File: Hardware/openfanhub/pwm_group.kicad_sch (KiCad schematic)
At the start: 5 parts, among them Q3 Q_NMOS_GSD, Q4 AO449

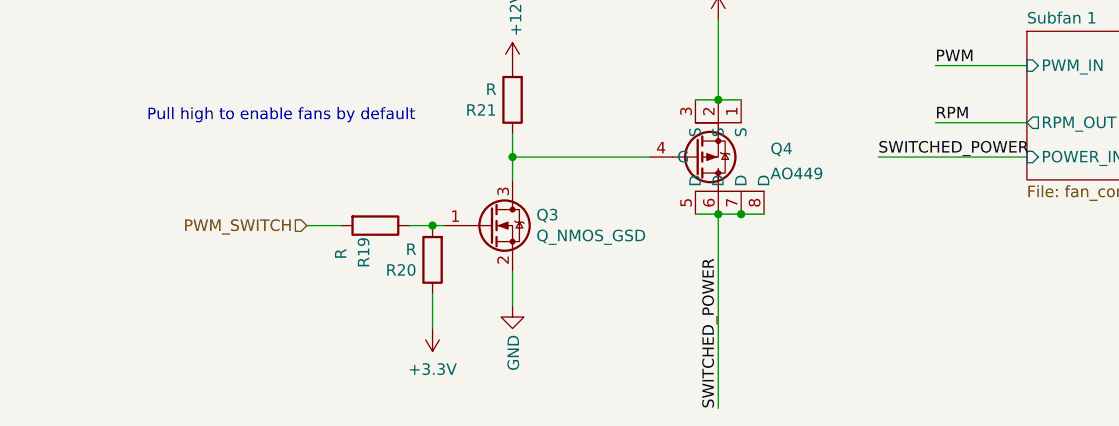
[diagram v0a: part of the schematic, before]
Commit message: Update PCB. Move Power and USB to the same side
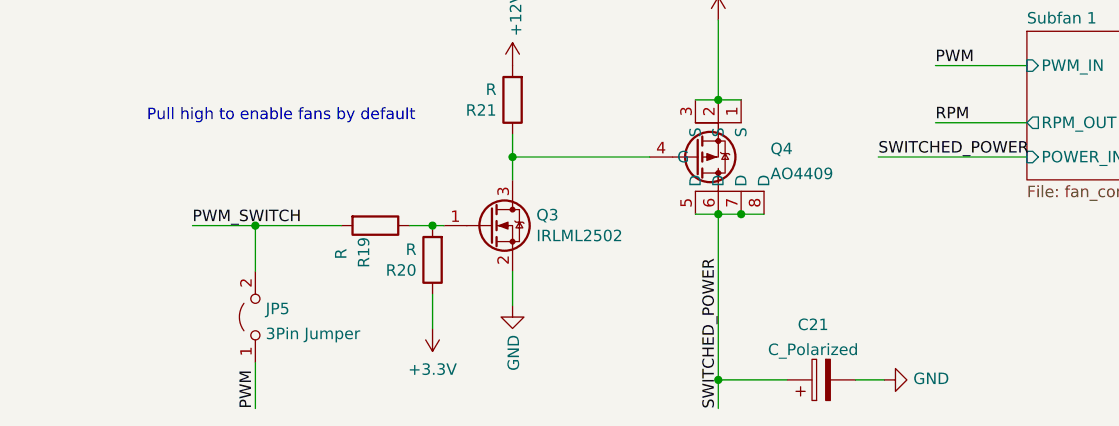
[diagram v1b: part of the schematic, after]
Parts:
- added C21: C_Polarized, Capacitor_THT:CP_Radial_D6.3mm_P2.50mm, symbol Device:C_Polarized
- added JP5: 3Pin Jumper, Connector_PinHeader_2.54mm:PinHeader_1x02_P2.54mm_Vertical, symbol Jumper:Jumper_2_Open
- Q3: value Q_NMOS_GSD -> IRLML2502
- Q4: value AO449 -> AO4409
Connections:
- net GND: now also C21.2
- net PWM: now also JP5.1 (A)
- net PWM_SWITCH: now also JP5.2 (B)
- net SWITCHED_POWER: now also C21.1
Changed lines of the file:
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@@
   (junction (at 71.12 58.42) (diameter 0) (color 0 0 0 0)
+  )
+  (junction (at 93.98 83.185) (diameter 0) (color 0 0 0 0)
+  )
+  (junction (at 42.545 66.04) (diameter 0) (color 0 0 0 0)
   )
   (junction (at 93.98 64.77) (diameter 0) (color 0 0 0 0)
@@
   (no_connect (at 170.18 55.88))
   (no_connect (at 213.36 55.88))
+  (wire (pts (xy 93.98 83.185) (xy 93.98 86.36))
+    (stroke (width 0) (type default) (color 0 0 0 0))
+  )
   (wire (pts (xy 152.4 59.69) (xy 170.18 59.69))
     (stroke (width 0) (type default) (color 0 0 0 0))
@@
     (stroke (width 0) (type default) (color 0 0 0 0))
   )
+  (wire (pts (xy 42.545 66.04) (xy 52.07 66.04))
+    (stroke (width 0) (type default) (color 0 0 0 0))
+  )
   (wire (pts (xy 93.98 52.07) (xy 96.52 52.07))
     (stroke (width 0) (type default) (color 0 0 0 0))
@@
     (stroke (width 0) (type default) (color 0 0 0 0))
   )
+  (wire (pts (xy 42.545 81.28) (xy 42.545 86.36))
+    (stroke (width 0) (type default) (color 0 0 0 0))
+  )
   (wire (pts (xy 111.76 58.42) (xy 128.27 58.42))
     (stroke (width 0) (type default) (color 0 0 0 0))
   )
-  (wire (pts (xy 48.26 66.04) (xy 52.07 66.04))
-    (stroke (width 0) (type default) (color 0 0 0 0))
-  )
-  (wire (pts (xy 93.98 64.77) (xy 93.98 86.36))
+  (wire (pts (xy 35.56 66.04) (xy 42.545 66.04))
+    (stroke (width 0) (type default) (color 0 0 0 0))
+  )
+  (wire (pts (xy 109.22 83.185) (xy 112.395 83.185))
+    (stroke (width 0) (type default) (color 0 0 0 0))
+  )
+  (wire (pts (xy 93.98 64.77) (xy 93.98 83.185))
     (stroke (width 0) (type default) (color 0 0 0 0))
   )
@@
     (stroke (width 0) (type default) (color 0 0 0 0))
   )
+  (wire (pts (xy 42.545 66.04) (xy 42.545 71.12))
+    (stroke (width 0) (type default) (color 0 0 0 0))
+  )
   (wire (pts (xy 162.56 49.53) (xy 170.18 49.53))
     (stroke (width 0) (type default) (color 0 0 0 0))
@@
     (stroke (width 0) (type default) (color 0 0 0 0))
   )
+  (wire (pts (xy 93.98 83.185) (xy 101.6 83.185))
+    (stroke (width 0) (type default) (color 0 0 0 0))
+  )
   (wire (pts (xy 93.98 43.18) (xy 93.98 52.07))
     (stroke (width 0) (type default) (color 0 0 0 0))
@@
   )
   (label "RPM" (at 118.11 54.61 0)
-    (effects (font (size 1.27 1.27)) (justify left bottom))
-  )
-  (label "SWITCHED_POWER" (at 93.98 86.36 90)
-    (effects (font (size 1.27 1.27)) (justify left bottom))
-  )
-  (label "SWITCHED_POWER" (at 194.31 59.69 0)
     (effects (font (size 1.27 1.27)) (justify left bottom))
   )
@@
     (effects (font (size 1.27 1.27)) (justify right bottom))
   )
+  (label "SWITCHED_POWER" (at 93.98 86.36 90)
+    (effects (font (size 1.27 1.27)) (justify left bottom))
+  )
+  (label "SWITCHED_POWER" (at 194.31 59.69 0)
+    (effects (font (size 1.27 1.27)) (justify left bottom))
+  )
+  (label "PWM_SWITCH" (at 35.56 66.04 0)
+    (effects (font (size 1.27 1.27)) (justify left bottom))
+  )
   (label "RPM" (at 41.91 24.13 180)
     (effects (font (size 1.27 1.27)) (justify right bottom))
@@
     (effects (font (size 1.27 1.27)) (justify right bottom))
   )
+  (label "PWM" (at 42.545 86.36 90)
+    (effects (font (size 1.27 1.27)) (justify left bottom))
+  )
   (label "PWM" (at 118.11 48.26 0)
     (effects (font (size 1.27 1.27)) (justify left bottom))
@@
     (effects (font (size 1.27 1.27)) (justify right))
   )
-  (hierarchical_label "PWM_SWITCH" (shape input) (at 48.26 66.04 180)
-    (effects (font (size 1.27 1.27)) (justify right))
-  )
   (symbol (lib_id "power:+12V") (at 93.98 43.18 0)
     (in_bom yes) (on_board yes)
-    (property "Reference" "#PWR086" (id 0) (at 93.98 46.99 0)
+    (property "Reference" "#PWR058" (id 0) (at 93.98 46.99 0)
       (effects (font (size 1.27 1.27)) hide)
     )
@@
   (symbol (lib_id "power:+12V") (at 71.12 48.26 0)
     (in_bom yes) (on_board yes)
-    (property "Reference" "#PWR084" (id 0) (at 71.12 52.07 0)
+    (property "Reference" "#PWR056" (id 0) (at 71.12 52.07 0)
       (effects (font (size 1.27 1.27)) hide)
     )
@@
       (effects (font (size 1.27 1.27)) (justify left))
     )
-    (property "Value" "Q_NMOS_GSD" (id 1) (at 73.7616 67.183 0)
+    (property "Value" "IRLML2502" (id 1) (at 73.7616 67.183 0)
       (effects (font (size 1.27 1.27)) (justify left))
     )
@@
   (symbol (lib_id "power:GND") (at 71.12 74.93 0)
     (in_bom yes) (on_board yes)
-    (property "Reference" "#PWR085" (id 0) (at 71.12 81.28 0)
+    (property "Reference" "#PWR057" (id 0) (at 71.12 81.28 0)
       (effects (font (size 1.27 1.27)) hide)
     )
@@
     (pin "1")
     (pin "2")
+  )
+  (symbol (lib_id "power:GND") (at 112.395 83.185 90)
+    (in_bom yes) (on_board yes)
+    (property "Reference" "#PWR059" (id 0) (at 118.745 83.185 0)
+      (effects (font (size 1.27 1.27)) hide)
+    )
+    (property "Value" "GND" (id 1) (at 115.6462 83.058 90)
+      (effects (font (size 1.27 1.27)) (justify right))
+    )
+    (property "Footprint" "" (id 2) (at 112.395 83.185 0)
+      (effects (font (size 1.27 1.27)) hide)
+    )
+    (property "Datasheet" "" (id 3) (at 112.395 83.185 0)
+      (effects (font (size 1.27 1.27)) hide)
+    )
+    (pin "1")
   )
   (symbol (lib_id "my_components:AO449") (at 82.55 63.5 0) (mirror x)
@@
       (effects (font (size 1.27 1.27)) (justify left))
     )
-    (property "Value" "AO449" (id 1) (at 99.7712 60.2866 0)
+    (property "Value" "AO4409" (id 1) (at 99.7712 60.2866 0)
       (effects (font (size 1.27 1.27)) (justify left))
     )
@@
   (symbol (lib_id "power:+3.3V") (at 62.23 77.47 180)
     (in_bom yes) (on_board yes) (fields_autoplaced)
-    (property "Reference" "#PWR083" (id 0) (at 62.23 73.66 0)
+    (property "Reference" "#PWR055" (id 0) (at 62.23 73.66 0)
       (effects (font (size 1.27 1.27)) hide)
     )
@@
     (pin "1")
   )
+  (symbol (lib_id "Device:C_Polarized") (at 105.41 83.185 90)
+    (in_bom yes) (on_board yes) (fields_autoplaced)
+    (property "Reference" "C21" (id 0) (at 104.521 77.0595 90))
+    (property "Value" "C_Polarized" (id 1) (at 104.521 79.8346 90))
+    (property "Footprint" "Capacitor_THT:CP_Radial_D6.3mm_P2.50mm" (id 2) (at 109.22 82.2198 0)
+      (effects (font (size 1.27 1.27)) hide)
+    )
+    (property "Datasheet" "~" (id 3) (at 105.41 83.185 0)
+      (effects (font (size 1.27 1.27)) hide)
+    )
+    (pin "1")
+    (pin "2")
+  )
+  (symbol (lib_id "Jumper:Jumper_2_Open") (at 42.545 76.2 90)
+    (in_bom yes) (on_board yes) (fields_autoplaced)
+    (property "Reference" "JP5" (id 0) (at 43.688 75.2915 90)
+      (effects (font (size 1.27 1.27)) (justify right))
+    )
+    (property "Value" "3Pin Jumper" (id 1) (at 43.688 78.0666 90)
+      (effects (font (size 1.27 1.27)) (justify right))
+    )
+    (property "Footprint" "Connector_PinHeader_2.54mm:PinHeader_1x02_P2.54mm_Vertical" (id 2) (at 42.545 76.2 0)
+      (effects (font (size 1.27 1.27)) hide)
+    )
+    (property "Datasheet" "~" (id 3) (at 42.545 76.2 0)
+      (effects (font (size 1.27 1.27)) hide)
+    )
+    (pin "1")
+    (pin "2")
+  )
   (sheet (at 128.27 44.45) (size 21.59 16.51) (fields_autoplaced)

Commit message: Update (not sure what)
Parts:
- renumbered C21 to C25, JP5 to JP9, Q3 to Q11, Q4 to Q12, R19 to R31, R20 to R32, R21 to R33
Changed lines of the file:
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@@
   (symbol (lib_id "power:+12V") (at 93.98 43.18 0)
     (in_bom yes) (on_board yes)
-    (property "Reference" "#PWR058" (id 0) (at 93.98 46.99 0)
+    (property "Reference" "#PWR090" (id 0) (at 93.98 46.99 0)
       (effects (font (size 1.27 1.27)) hide)
     )
@@
   (symbol (lib_id "Device:R") (at 55.88 66.04 270)
     (in_bom yes) (on_board yes)
-    (property "Reference" "R19" (id 0) (at 54.61 67.31 0)
+    (property "Reference" "R31" (id 0) (at 54.61 67.31 0)
       (effects (font (size 1.27 1.27)) (justify left))
     )
@@
   (symbol (lib_id "power:+12V") (at 71.12 48.26 0)
     (in_bom yes) (on_board yes)
-    (property "Reference" "#PWR056" (id 0) (at 71.12 52.07 0)
+    (property "Reference" "#PWR088" (id 0) (at 71.12 52.07 0)
       (effects (font (size 1.27 1.27)) hide)
     )
@@
   (symbol (lib_id "Device:Q_NMOS_GSD") (at 68.58 66.04 0)
     (in_bom yes) (on_board yes)
-    (property "Reference" "Q3" (id 0) (at 73.7616 64.8716 0)
+    (property "Reference" "Q11" (id 0) (at 73.7616 64.8716 0)
       (effects (font (size 1.27 1.27)) (justify left))
     )
@@
   (symbol (lib_id "Device:R") (at 71.12 52.07 180)
     (in_bom yes) (on_board yes)
-    (property "Reference" "R21" (id 0) (at 69.342 53.2384 0)
+    (property "Reference" "R33" (id 0) (at 69.342 53.2384 0)
       (effects (font (size 1.27 1.27)) (justify left))
     )
@@
   (symbol (lib_id "power:GND") (at 71.12 74.93 0)
     (in_bom yes) (on_board yes)
-    (property "Reference" "#PWR057" (id 0) (at 71.12 81.28 0)
+    (property "Reference" "#PWR089" (id 0) (at 71.12 81.28 0)
       (effects (font (size 1.27 1.27)) hide)
     )
@@
   (symbol (lib_id "Device:R") (at 62.23 69.85 180)
     (in_bom yes) (on_board yes)
-    (property "Reference" "R20" (id 0) (at 60.452 71.0184 0)
+    (property "Reference" "R32" (id 0) (at 60.452 71.0184 0)
       (effects (font (size 1.27 1.27)) (justify left))
     )
@@
   (symbol (lib_id "power:GND") (at 112.395 83.185 90)
     (in_bom yes) (on_board yes)
-    (property "Reference" "#PWR059" (id 0) (at 118.745 83.185 0)
+    (property "Reference" "#PWR091" (id 0) (at 118.745 83.185 0)
       (effects (font (size 1.27 1.27)) hide)
     )
@@
   (symbol (lib_id "my_components:AO449") (at 82.55 63.5 0) (mirror x)
     (in_bom yes) (on_board yes) (fields_autoplaced)
-    (property "Reference" "Q4" (id 0) (at 99.7712 57.5115 0)
+    (property "Reference" "Q12" (id 0) (at 99.7712 57.5115 0)
       (effects (font (size 1.27 1.27)) (justify left))
     )
@@
   (symbol (lib_id "power:+3.3V") (at 62.23 77.47 180)
     (in_bom yes) (on_board yes) (fields_autoplaced)
-    (property "Reference" "#PWR055" (id 0) (at 62.23 73.66 0)
+    (property "Reference" "#PWR087" (id 0) (at 62.23 73.66 0)
       (effects (font (size 1.27 1.27)) hide)
     )
@@
   (symbol (lib_id "Device:C_Polarized") (at 105.41 83.185 90)
     (in_bom yes) (on_board yes) (fields_autoplaced)
-    (property "Reference" "C21" (id 0) (at 104.521 77.0595 90))
+    (property "Reference" "C25" (id 0) (at 104.521 77.0595 90))
     (property "Value" "C_Polarized" (id 1) (at 104.521 79.8346 90))
     (property "Footprint" "Capacitor_THT:CP_Radial_D6.3mm_P2.50mm" (id 2) (at 109.22 82.2198 0)
@@
   (symbol (lib_id "Jumper:Jumper_2_Open") (at 42.545 76.2 90)
     (in_bom yes) (on_board yes) (fields_autoplaced)
-    (property "Reference" "JP5" (id 0) (at 43.688 75.2915 90)
+    (property "Reference" "JP9" (id 0) (at 43.688 75.2915 90)
       (effects (font (size 1.27 1.27)) (justify right))
     )

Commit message: update
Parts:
- renumbered C25 to C21, JP9 to JP5, Q11 to Q3, Q12 to Q4, R31 to R19, R32 to R20, R33 to R21
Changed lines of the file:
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@@
   (symbol (lib_id "Device:R") (at 55.88 66.04 270)
     (in_bom yes) (on_board yes)
-    (property "Reference" "R31" (id 0) (at 54.61 67.31 0)
+    (property "Reference" "R19" (id 0) (at 54.61 67.31 0)
       (effects (font (size 1.27 1.27)) (justify left))
     )
@@
   (symbol (lib_id "Device:Q_NMOS_GSD") (at 68.58 66.04 0)
     (in_bom yes) (on_board yes)
-    (property "Reference" "Q11" (id 0) (at 73.7616 64.8716 0)
+    (property "Reference" "Q3" (id 0) (at 73.7616 64.8716 0)
       (effects (font (size 1.27 1.27)) (justify left))
     )
@@
   (symbol (lib_id "Device:R") (at 71.12 52.07 180)
     (in_bom yes) (on_board yes)
-    (property "Reference" "R33" (id 0) (at 69.342 53.2384 0)
+    (property "Reference" "R21" (id 0) (at 69.342 53.2384 0)
       (effects (font (size 1.27 1.27)) (justify left))
     )
@@
   (symbol (lib_id "Device:R") (at 62.23 69.85 180)
     (in_bom yes) (on_board yes)
-    (property "Reference" "R32" (id 0) (at 60.452 71.0184 0)
+    (property "Reference" "R20" (id 0) (at 60.452 71.0184 0)
       (effects (font (size 1.27 1.27)) (justify left))
     )
@@
   (symbol (lib_id "my_components:AO449") (at 82.55 63.5 0) (mirror x)
     (in_bom yes) (on_board yes) (fields_autoplaced)
-    (property "Reference" "Q12" (id 0) (at 99.7712 57.5115 0)
+    (property "Reference" "Q4" (id 0) (at 99.7712 57.5115 0)
       (effects (font (size 1.27 1.27)) (justify left))
     )
@@
   (symbol (lib_id "Device:C_Polarized") (at 105.41 83.185 90)
     (in_bom yes) (on_board yes) (fields_autoplaced)
-    (property "Reference" "C25" (id 0) (at 104.521 77.0595 90))
+    (property "Reference" "C21" (id 0) (at 104.521 77.0595 90))
     (property "Value" "C_Polarized" (id 1) (at 104.521 79.8346 90))
     (property "Footprint" "Capacitor_THT:CP_Radial_D6.3mm_P2.50mm" (id 2) (at 109.22 82.2198 0)
@@
   (symbol (lib_id "Jumper:Jumper_2_Open") (at 42.545 76.2 90)
     (in_bom yes) (on_board yes) (fields_autoplaced)
-    (property "Reference" "JP9" (id 0) (at 43.688 75.2915 90)
+    (property "Reference" "JP5" (id 0) (at 43.688 75.2915 90)
       (effects (font (size 1.27 1.27)) (justify right))
     )
